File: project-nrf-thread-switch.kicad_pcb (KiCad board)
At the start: 2 copper layers, 149.9 x 30.5 mm, 14 parts, among them J1 Left, J2 Right

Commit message: Add power_sym
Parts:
- added Ref**: Val**, project-nrf-thread-switch_hardware:power_sym, F.Cu at (135.9, 30.5)

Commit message: Add previous commit version
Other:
- board text added: "François Gervais 18 mars 2022 v1.0"

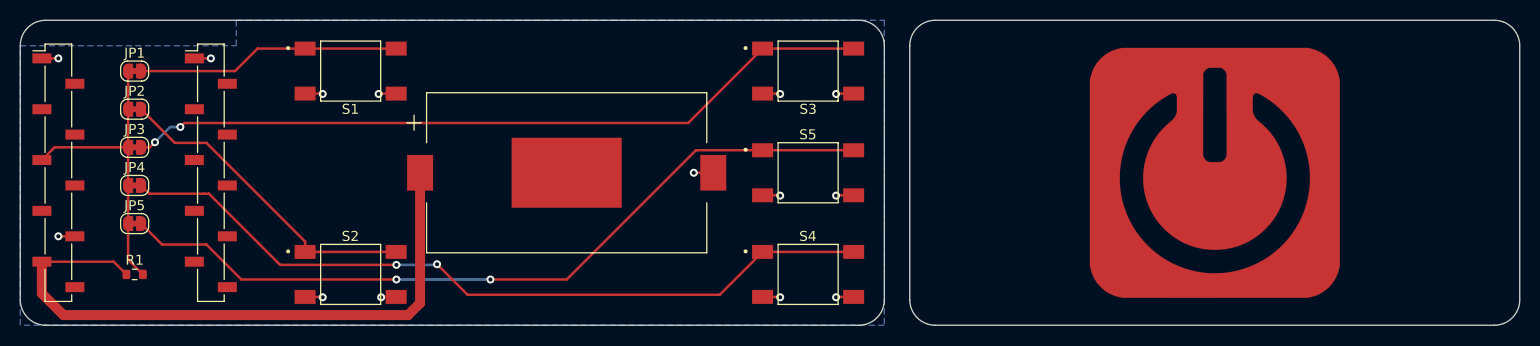
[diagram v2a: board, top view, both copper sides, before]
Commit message: Single button with header footprint fix
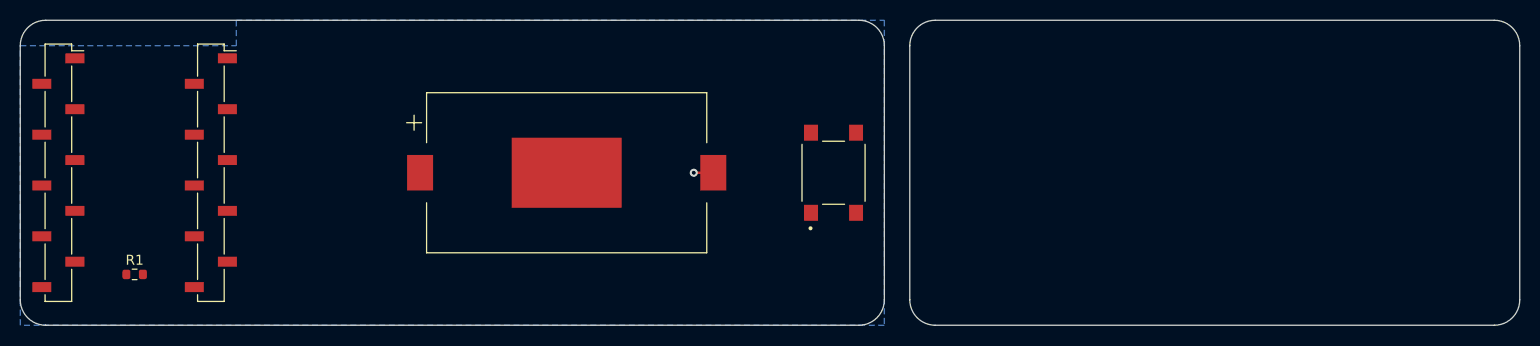
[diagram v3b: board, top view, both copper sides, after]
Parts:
- removed JP1, JP2, JP3, JP4, JP5: Jumper_2_Bridged, Jumper:SolderJumper-2_P1.3mm_Bridged_RoundedPad1.0x1.5mm
- removed Ref**: Val**, project-nrf-thread-switch_hardware:power_sym
- removed S2, S3, S4, S5: 1571563-9, 1571563-9:SW_1571563-9
- J1, J2: footprint Connector_PinSocket_2.54mm:PinSocket_1x10_P2.54mm_Vertical_SMD_Pin1Left -> Connector_PinSocket_2.54mm:PinSocket_1x10_P2.54mm_Vertical_SMD_Pin1Right
- S1: footprint 1571563-9:SW_1571563-9 -> B3FS-1010:SW_B3FS-1010P
- moved S1 49.3 mm to (97.8, 30.5), turned to 90 degrees
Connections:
- S1 pad 1: Net-(JP1-Pad2) -> /0.02
- S1 pad 2: Net-(JP1-Pad2) -> /0.02
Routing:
- net Net-(JP5-Pad2): track 78.9 -> 0.00 mm, vias 2 -> 0
- net Net-(JP4-Pad2): track 77.6 -> 0.00 mm, vias 2 -> 0
- net Net-(JP3-Pad2): track 75.3 -> 0.00 mm, vias 2 -> 0
- net VCC: track 64.4 -> 0.00 mm
- net Net-(JP2-Pad2): track 32.0 -> 0.00 mm
- net /0.02: track 30.1 -> 0.00 mm
- net Net-(JP1-Pad2): track 26.4 -> 0.00 mm
- net GND: track 24.4 -> 1.95 mm, vias 14 -> 1

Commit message: Routing done
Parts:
- added Ref**: Val**, project-nrf-thread-switch_hardware:power_sym, F.Cu at (135.9, 30.5)
- moved BT1 3.81 mm to (74.9, 30.5)
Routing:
- net /0.02: track 0.00 -> 104.2 mm
- net VCC: track 0.00 -> 53.5 mm
- net GND: track 1.95 -> 9.85 mm, vias 1 -> 6
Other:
- board text added: "François Gervais et Julie Gervais 25 mars 2022 v"
- board text removed: "François Gervais 18 mars 2022 v1.0"

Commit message: Add previous commit version
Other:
- board text added: "François Gervais et Julie Gervais 25 mars 2022 v1.0-4-gb91c259"
- board text removed: "François Gervais et Julie Gervais 25 mars 2022 v"
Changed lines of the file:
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@@
     )
   )
-  (gr_text "François Gervais et Julie Gervais\n25 mars 2022\nv" (at 164.084 19.05) (layer B.SilkS)
+  (gr_text "François Gervais et Julie Gervais\n25 mars 2022\nv1.0-4-gb91c259" (at 164.084 19.05) (layer B.SilkS)
     (effects (font (size 1 1) (thickness 0.15)) (justify left mirror))
   )

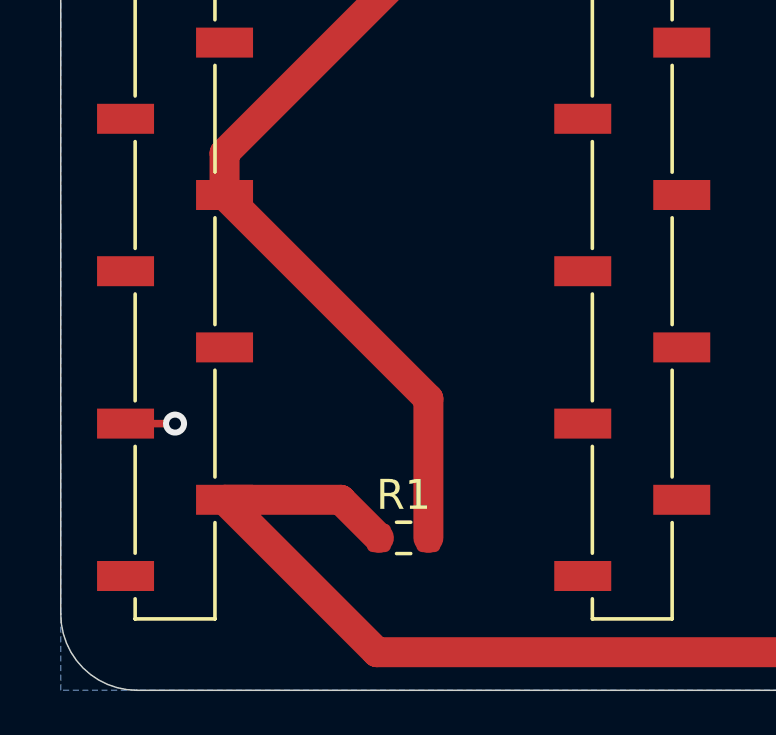
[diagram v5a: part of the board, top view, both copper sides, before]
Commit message: Move pull-up
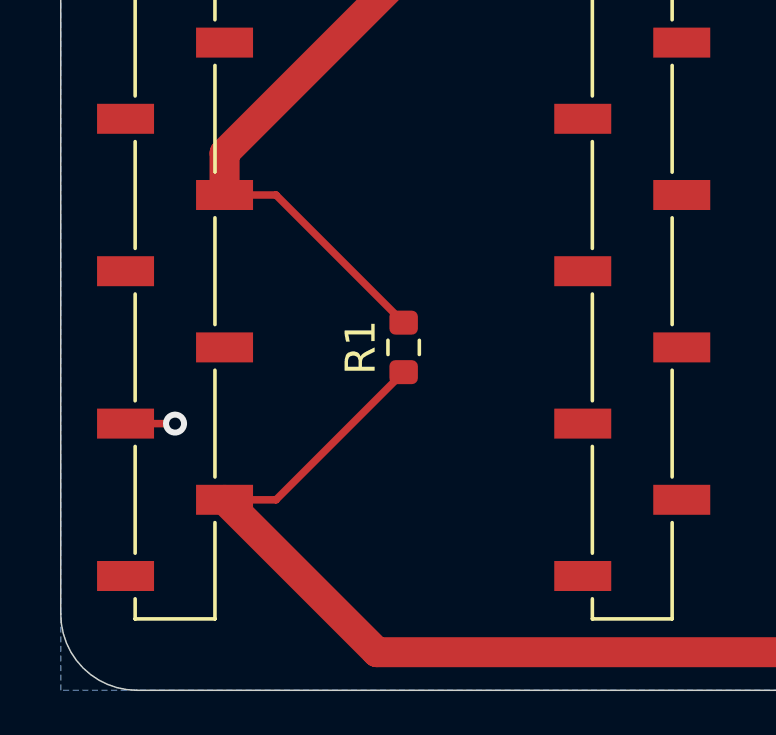
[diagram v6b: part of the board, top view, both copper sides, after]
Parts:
- moved R1 6.35 mm to (27.9, 34.3), turned to 90 degrees
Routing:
- net /0.02: track 104.2 -> 97.7 mm
- net VCC: track 53.5 -> 55.6 mm

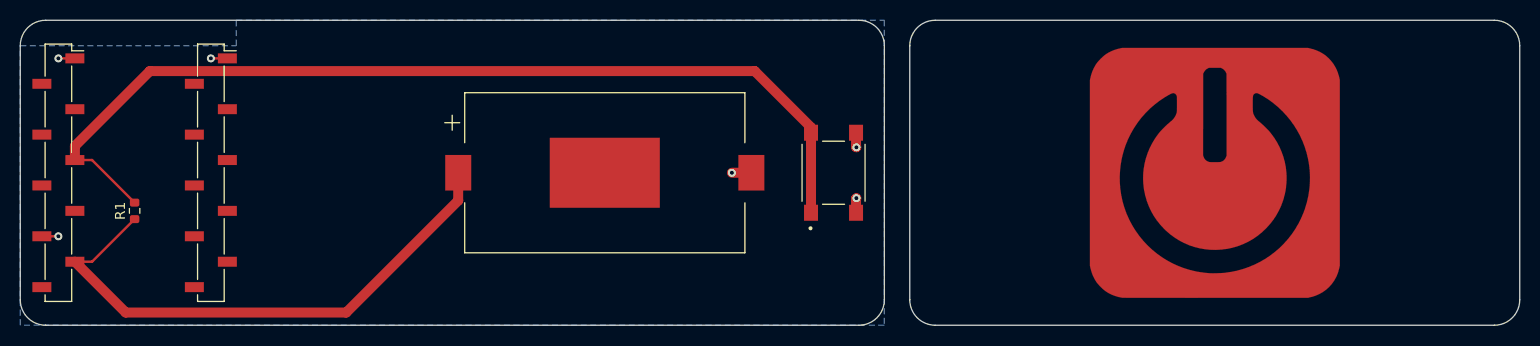
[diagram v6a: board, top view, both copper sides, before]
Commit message: Make track slimmer
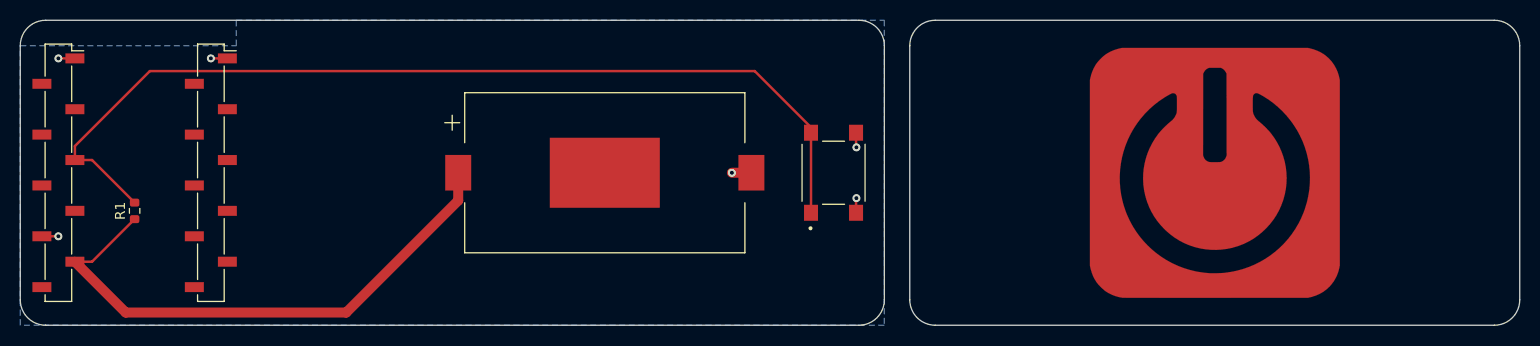
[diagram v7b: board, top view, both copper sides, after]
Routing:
- net /0.02: track 97.7 -> 96.1 mm
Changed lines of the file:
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@@
     (thickness 1.6)
     (drawings 17)
-    (tracks 29)
+    (tracks 27)
     (zones 0)
     (modules 6)
@@
   (segment (start 89.58 30.48) (end 87.63 30.48) (width 1) (layer F.Cu) (net 1))
   (via (at 100.076 33.02) (size 0.8) (drill 0.4) (layers F.Cu B.Cu) (net 1))
-  (segment (start 100.04 34.48) (end 100.04 33.056) (width 1) (layer F.Cu) (net 1))
-  (segment (start 100.04 33.056) (end 100.076 33.02) (width 1) (layer F.Cu) (net 1))
-  (segment (start 100.04 26.48) (end 100.04 27.904) (width 1) (layer F.Cu) (net 1))
   (via (at 100.076 27.94) (size 0.8) (drill 0.4) (layers F.Cu B.Cu) (net 1))
-  (segment (start 100.04 27.904) (end 100.076 27.94) (width 1) (layer F.Cu) (net 1))
   (via (at 20.32 36.83) (size 0.8) (drill 0.4) (layers F.Cu B.Cu) (net 1))
   (segment (start 18.67 36.83) (end 20.32 36.83) (width 0.25) (layer F.Cu) (net 1))
+  (segment (start 100.04 27.904) (end 100.076 27.94) (width 0.25) (layer F.Cu) (net 1))
+  (segment (start 100.04 26.48) (end 100.04 27.904) (width 0.25) (layer F.Cu) (net 1))
+  (segment (start 100.04 33.056) (end 100.076 33.02) (width 0.25) (layer F.Cu) (net 1))
+  (segment (start 100.04 34.48) (end 100.04 33.056) (width 0.25) (layer F.Cu) (net 1))
   (segment (start 60.28 33.26) (end 49.09 44.45) (width 1) (layer F.Cu) (net 2))
   (segment (start 60.28 30.48) (end 60.28 33.26) (width 1) (layer F.Cu) (net 2))
@@
   (segment (start 23.685 39.37) (end 27.94 35.115) (width 0.25) (layer F.Cu) (net 2))
   (segment (start 21.97 39.37) (end 23.685 39.37) (width 0.25) (layer F.Cu) (net 2))
-  (segment (start 95.54 27.468) (end 95.54 25.944) (width 1) (layer F.Cu) (net 8))
-  (segment (start 95.54 34.48) (end 95.54 27.468) (width 1) (layer F.Cu) (net 8))
-  (segment (start 95.54 27.468) (end 95.54 26.48) (width 1) (layer F.Cu) (net 8))
-  (segment (start 95.54 25.944) (end 89.916 20.32) (width 1) (layer F.Cu) (net 8))
-  (segment (start 89.916 20.32) (end 29.464 20.32) (width 1) (layer F.Cu) (net 8))
-  (segment (start 21.97 27.814) (end 21.97 29.21) (width 1) (layer F.Cu) (net 8))
-  (segment (start 29.464 20.32) (end 21.97 27.814) (width 1) (layer F.Cu) (net 8))
   (segment (start 23.685 29.21) (end 27.94 33.465) (width 0.25) (layer F.Cu) (net 8))
   (segment (start 21.97 29.21) (end 23.685 29.21) (width 0.25) (layer F.Cu) (net 8))
+  (segment (start 29.464 20.32) (end 21.97 27.814) (width 0.25) (layer F.Cu) (net 8))
+  (segment (start 95.54 25.944) (end 89.916 20.32) (width 0.25) (layer F.Cu) (net 8))
+  (segment (start 89.916 20.32) (end 29.464 20.32) (width 0.25) (layer F.Cu) (net 8))
+  (segment (start 21.97 27.814) (end 21.97 29.21) (width 0.25) (layer F.Cu) (net 8))
+  (segment (start 95.54 34.48) (end 95.54 26.48) (width 0.25) (layer F.Cu) (net 8))
   (zone (net 1) (net_name GND) (layer B.Cu) (hatch edge 0.508)
     (connect_pads (clearance 0.508))

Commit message: Add previous commit version
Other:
- board text added: "François Gervais et Julie Gervais 25 mars 2022 v1.0-7-ge5c6c3e"
- board text removed: "François Gervais et Julie Gervais 25 mars 2022 v1.0-4-gb91c259"
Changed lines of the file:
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@@
     )
   )
-  (gr_text "François Gervais et Julie Gervais\n25 mars 2022\nv1.0-4-gb91c259" (at 164.084 19.05) (layer B.SilkS)
+  (gr_text "François Gervais et Julie Gervais\n25 mars 2022\nv1.0-7-ge5c6c3e" (at 164.084 19.05) (layer B.SilkS)
     (effects (font (size 1 1) (thickness 0.15)) (justify left mirror))
   )
